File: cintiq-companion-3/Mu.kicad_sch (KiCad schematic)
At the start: 12 parts, among them J1 Conn_01x03_Pin

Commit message: susclk
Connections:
- net SUSCLK_WIFI: now also A1.131 (SUSCLK)
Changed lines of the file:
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@@
 	(wire
 		(pts
+			(xy 427.99 158.75) (xy 445.77 158.75)
+		)
+		(stroke
+			(width 0)
+			(type default)
+		)
+	)
+	(wire
+		(pts
 			(xy 427.99 120.65) (xy 495.3 120.65)
 		)
@@
 	(global_label "SUSCLK_WIFI"
 		(shape input)
-		(at 466.09 158.75 0)
+		(at 445.77 158.75 0)
 		(fields_autoplaced yes)
 		(effects
@@
 		)
 		(property "Intersheetrefs" "${INTERSHEET_REFS}"
-			(at 466.09 158.75 0)
+			(at 445.77 158.75 0)
 			(effects
 				(font
@@
 			(effects
 				(font
-					(size 1.27 1.27)
+					(size 1.016 1.016)
 				)
 				(hide yes)
@@
 			(effects
 				(font
-					(size 1.27 1.27)
+					(size 1.016 1.016)
 				)
 			)
@@
 			(effects
 				(font
-					(size 1.27 1.27)
+					(size 1.016 1.016)
 				)
 			)
@@
 			(effects
 				(font
-					(size 1 1)
+					(size 1.016 1.016)
 				)
 			)
@@
 			(effects
 				(font
-					(size 1.27 1.27)
+					(size 1.016 1.016)
 				)
 				(hide yes)
@@
 			(effects
 				(font
-					(size 1.27 1.27)
+					(size 1.016 1.016)
 				)
 			)
@@
 			(effects
 				(font
-					(size 1.27 1.27)
+					(size 1.016 1.016)
 				)
 				(justify left)
@@
 			(effects
 				(font
-					(size 1.27 1.27)
+					(size 1.016 1.016)
 				)
 				(justify left)
@@
 			(effects
 				(font
-					(size 1.27 1.27)
+					(size 1.016 1.016)
 				)
 			)
@@
 			(effects
 				(font
-					(size 1 1)
+					(size 1.016 1.016)
 				)
 			)
@@
 			(effects
 				(font
-					(size 1.27 1.27)
+					(size 1.016 1.016)
 				)
 				(hide yes)
@@
 			(effects
 				(font
-					(size 1.27 1.27)
+					(size 1.016 1.016)
 				)
 			)
@@
 			(effects
 				(font
-					(size 1.27 1.27)
+					(size 1.016 1.016)
 				)
 				(justify left)
@@
 			(effects
 				(font
-					(size 1.27 1.27)
+					(size 1.016 1.016)
 				)
 				(justify left)
@@
 			(effects
 				(font
-					(size 1.27 1.27)
+					(size 1.016 1.016)
 				)
 				(hide yes)
@@
 			(effects
 				(font
-					(size 1.27 1.27)
+					(size 1.016 1.016)
 				)
 				(justify left)
@@
 			(effects
 				(font
-					(size 1.27 1.27)
+					(size 1.016 1.016)
 				)
 				(justify left)
@@
 			(effects
 				(font
-					(size 1.27 1.27)
+					(size 1.016 1.016)
 				)
 				(justify left)
@@
 			(effects
 				(font
-					(size 1.27 1.27)
+					(size 1.016 1.016)
 				)
 				(hide yes)
@@
 			(effects
 				(font
-					(size 1.27 1.27)
+					(size 1.016 1.016)
 				)
 			)
@@
 			(effects
 				(font
-					(size 1.27 1.27)
+					(size 1.016 1.016)
 				)
 				(justify left)
@@
 			(effects
 				(font
-					(size 1.27 1.27)
+					(size 1.016 1.016)
 				)
 				(justify left)
@@
 			(effects
 				(font
-					(size 1.27 1.27)
+					(size 1.016 1.016)
 				)
 				(justify left)
@@
 			(effects
 				(font
-					(size 1.27 1.27)
+					(size 1.016 1.016)
 				)
 				(justify left)
@@
 			(effects
 				(font
-					(size 1 1)
+					(size 1.016 1.016)
 				)
 			)
@@
 			(effects
 				(font
-					(size 1 1)
+					(size 1.016 1.016)
 				)
 			)
@@
 			(effects
 				(font
-					(size 1.27 1.27)
+					(size 1.016 1.016)
 				)
 				(hide yes)
@@
 			(effects
 				(font
-					(size 1.27 1.27)
+					(size 1.016 1.016)
 				)
 				(justify right)
@@
 			(effects
 				(font
-					(size 1.27 1.27)
+					(size 1.016 1.016)
 				)
 				(hide yes)
@@
 			(effects
 				(font
-					(size 1.27 1.27)
+					(size 1.016 1.016)
 				)
 				(justify right)
@@
 			(effects
 				(font
-					(size 1.27 1.27)
+					(size 1.016 1.016)
 				)
 				(hide yes)
@@
 			(effects
 				(font
-					(size 1.27 1.27)
+					(size 1.016 1.016)
 				)
 			)
@@
 			(effects
 				(font
-					(size 1.27 1.27)
+					(size 1.016 1.016)
 				)
 				(hide yes)
@@
 			(effects
 				(font
-					(size 1.27 1.27)
+					(size 1.016 1.016)
 				)
 			)
@@
 			(effects
 				(font
-					(size 1 1)
+					(size 1.016 1.016)
 				)
 				(justify left)
@@
 			(effects
 				(font
-					(size 1 1)
+					(size 1.016 1.016)
 				)
 				(justify left)
@@
 			(effects
 				(font
-					(size 1.27 1.27)
+					(size 1.016 1.016)
 				)
 				(hide yes)
@@
 			(effects
 				(font
-					(size 1.27 1.27)
+					(size 1.016 1.016)
 				)
 			)
@@
 			(effects
 				(font
-					(size 1.27 1.27)
+					(size 1.016 1.016)
 				)
 				(hide yes)
@@
 			(effects
 				(font
-					(size 1.27 1.27)
+					(size 1.016 1.016)
 				)
 			)
@@
 			(effects
 				(font
-					(size 1.27 1.27)
+					(size 1.016 1.016)
 				)
 				(hide yes)
@@
 			(effects
 				(font
-					(size 1.27 1.27)
+					(size 1.016 1.016)
 				)
 			)
@@
 			(effects
 				(font
-					(size 1.27 1.27)
+					(size 1.016 1.016)
 				)
 				(justify left)
@@
 			(effects
 				(font
-					(size 1.27 1.27)
+					(size 1.016 1.016)
 				)
 				(justify left)
@@
 			(effects
 				(font
-					(size 1.27 1.27)
+					(size 1.016 1.016)
 				)
 				(hide yes)
@@
 			(effects
 				(font
-					(size 1.27 1.27)
+					(size 1.016 1.016)
 				)
 			)
@@
 			(effects
 				(font
-					(size 1.27 1.27)
+					(size 1.016 1.016)
 				)
 				(justify left)
@@
 			(effects
 				(font
-					(size 1.27 1.27)
+					(size 1.016 1.016)
 				)
 				(justify left)
@@
 			(effects
 				(font
-					(size 1.27 1.27)
+					(size 1.016 1.016)
 				)
 			)
@@
 			(effects
 				(font
-					(size 1.27 1.27)
+					(size 1.016 1.016)
 				)
 			)

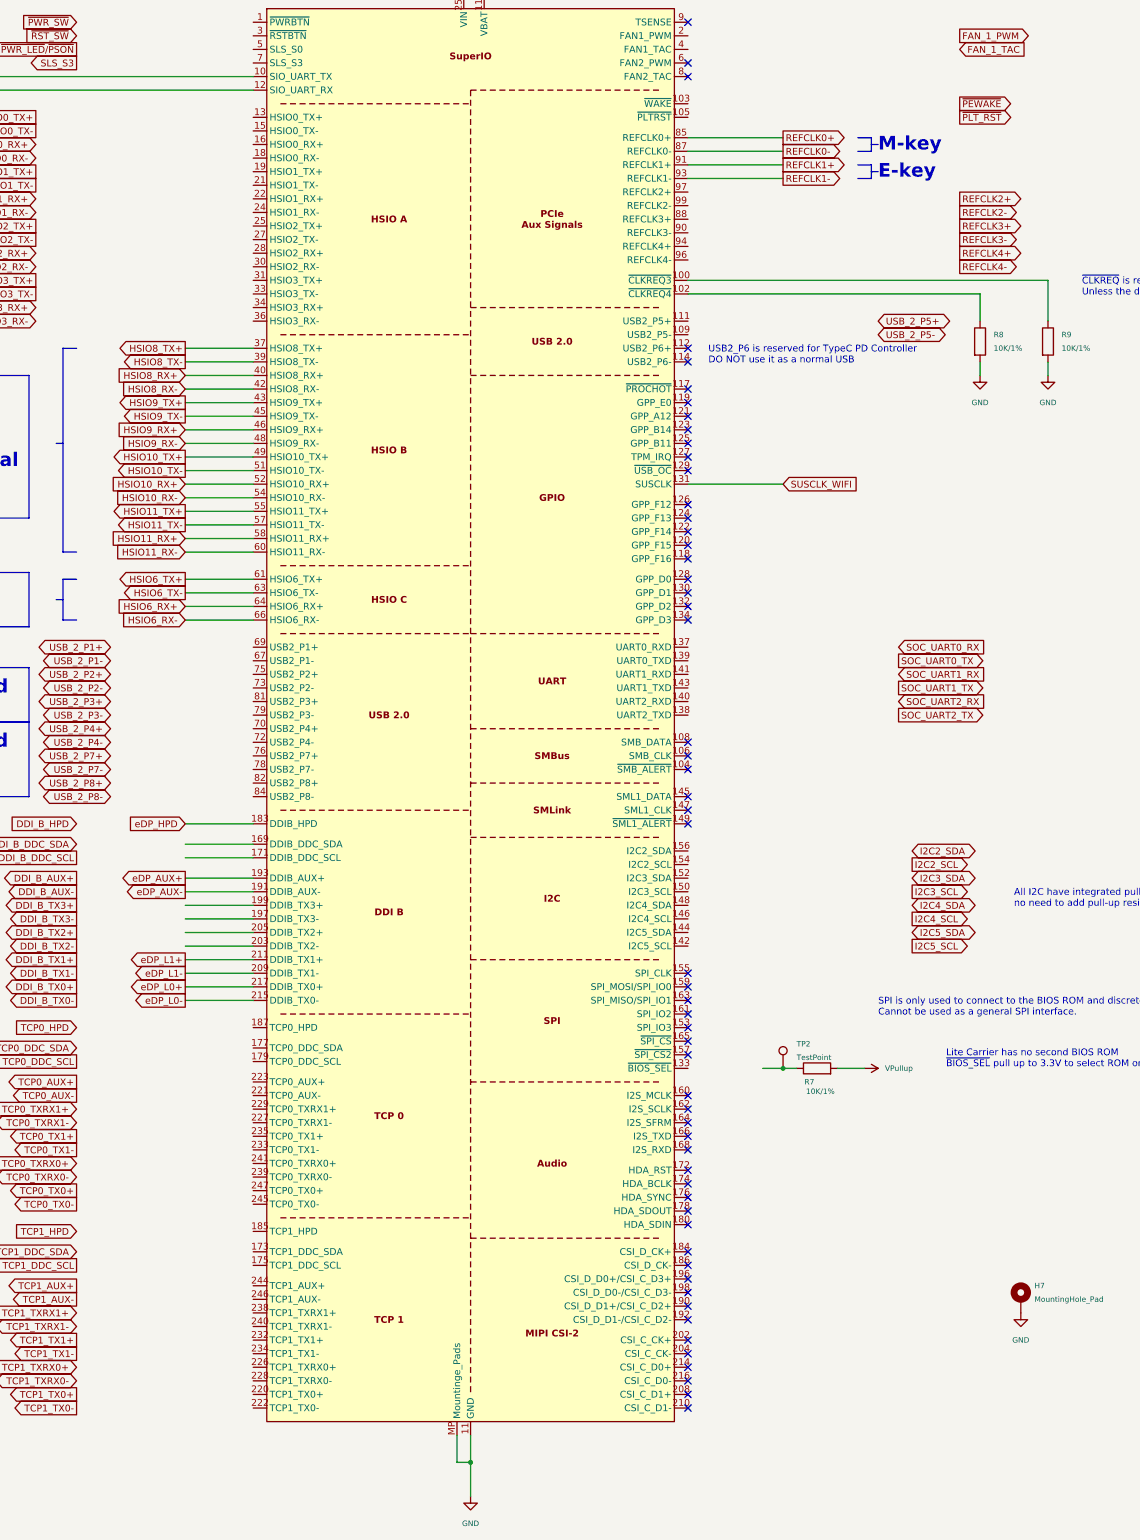
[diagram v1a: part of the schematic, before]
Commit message: renamed pcie nets
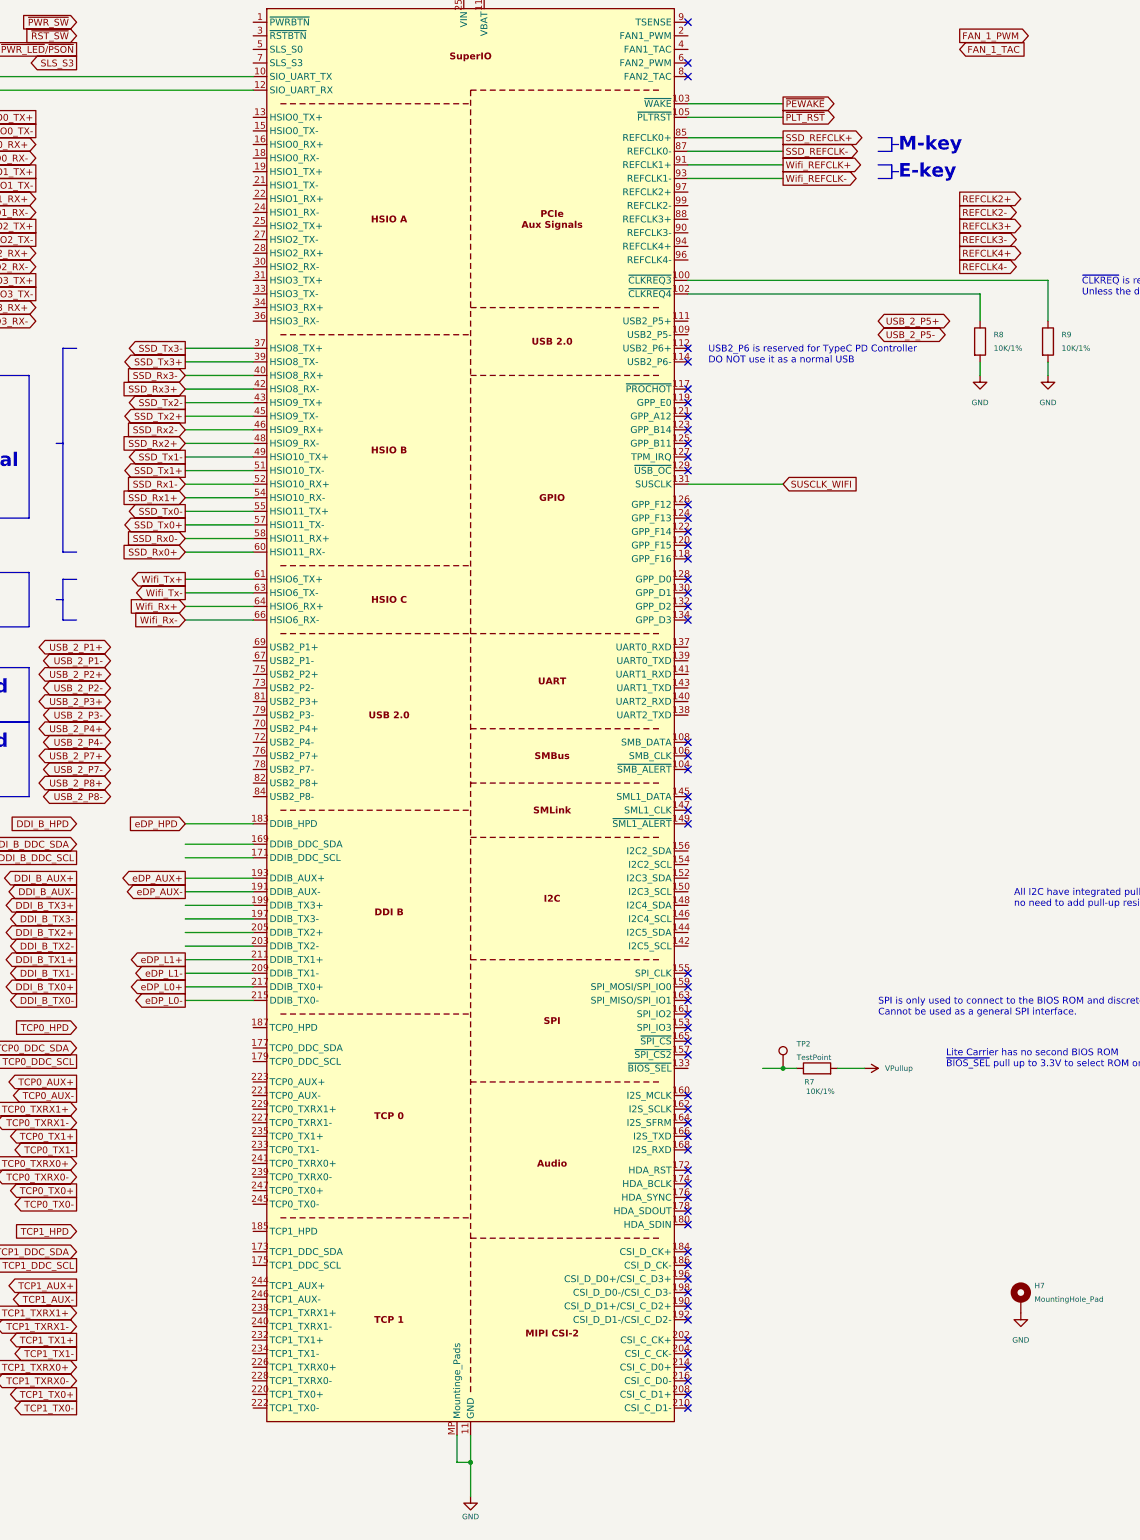
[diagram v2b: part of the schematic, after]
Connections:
- net ~{PEWAKE}: now also A1.103 (~{WAKE})
- net ~{PLT_RST}: now also A1.105 (~{PLTRST})
- net HSIO10_RX+ renamed SSD_Rx1-
- net HSIO10_RX- renamed SSD_Rx1+
- net HSIO10_TX+ renamed SSD_Tx1-
- net HSIO10_TX- renamed SSD_Tx1+
- net HSIO11_RX+ renamed SSD_Rx0-
- net HSIO11_RX- renamed SSD_Rx0+
- net HSIO11_TX+ renamed SSD_Tx0-
- net HSIO11_TX- renamed SSD_Tx0+
- net HSIO6_RX+ renamed Wifi_Rx+
- net HSIO6_RX- renamed Wifi_Rx-
- net HSIO6_TX+ renamed Wifi_Tx+
- net HSIO6_TX- renamed Wifi_Tx-
- net HSIO8_RX+ renamed SSD_Rx3-
- net HSIO8_RX- renamed SSD_Rx3+
- net HSIO8_TX+ renamed SSD_Tx3-
- net HSIO8_TX- renamed SSD_Tx3+
- net HSIO9_RX+ renamed SSD_Rx2-
- net HSIO9_RX- renamed SSD_Rx2+
- net HSIO9_TX+ renamed SSD_Tx2-
- net HSIO9_TX- renamed SSD_Tx2+
- net REFCLK0+ renamed SSD_REFCLK+
- net REFCLK0- renamed SSD_REFCLK-
- net REFCLK1+ renamed Wifi_REFCLK+
- net REFCLK1- renamed Wifi_REFCLK-
